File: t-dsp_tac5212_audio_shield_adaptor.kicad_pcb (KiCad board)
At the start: 2 copper layers, 26.5 x 60.9 mm, 22 parts, among them U1 Teensy 4.1 - DEVKIT

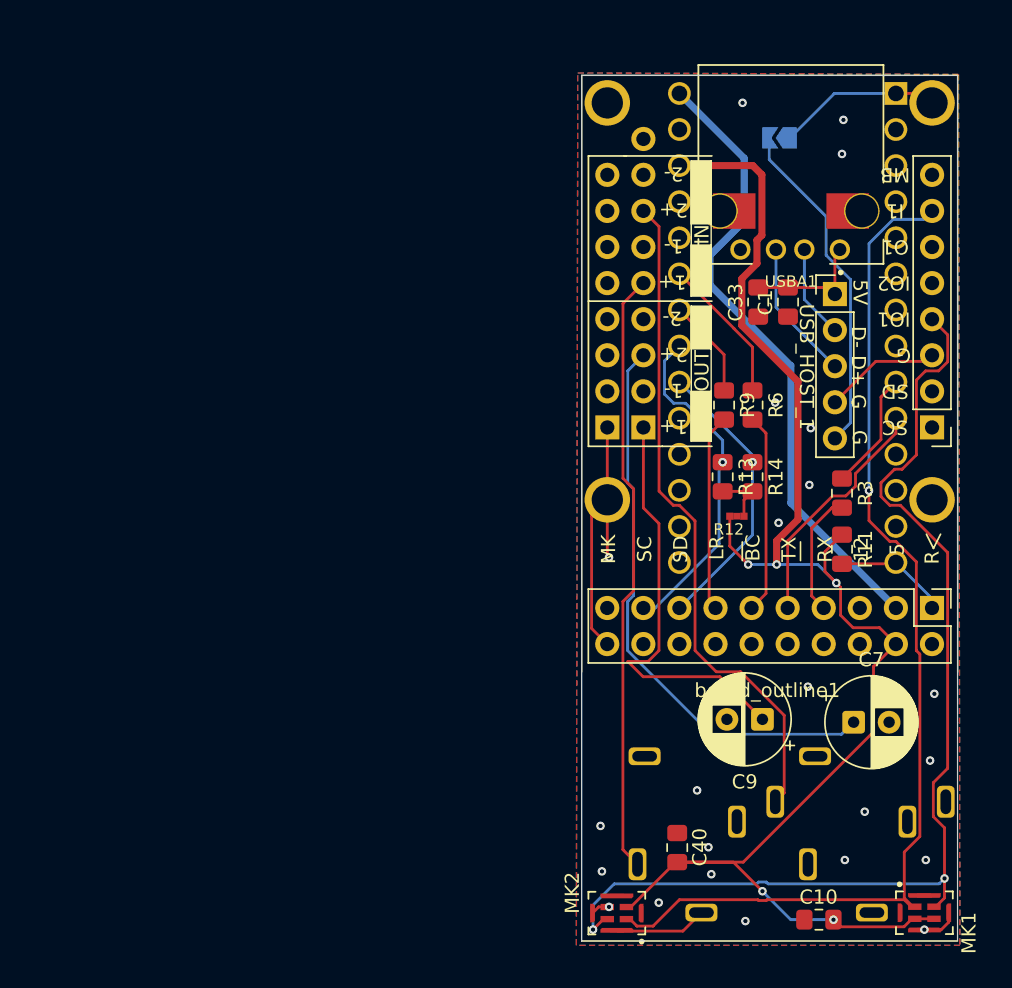
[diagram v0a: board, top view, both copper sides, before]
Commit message: v0.1: Finish routing, update board outline and revision
- Complete PCB routing and zone fills
- Add board outline footprint variants (-0.66mm offset)
- Update USB-A footprint to KiCad 9.0 format
- Fix schematic connections and capacitor orientation
- Correct project filename metadata
- Update 3D model
- Set REVISION to v0.1
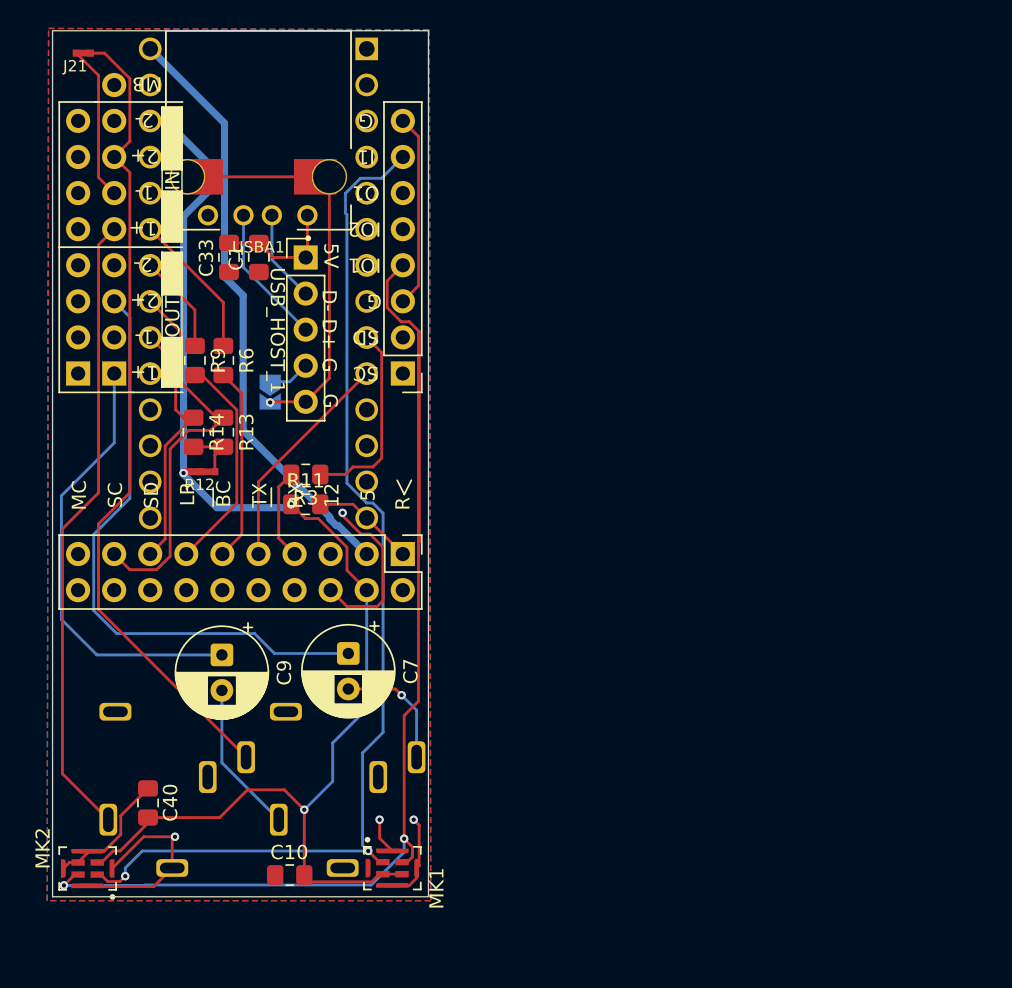
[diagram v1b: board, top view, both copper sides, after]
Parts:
- added J21: jumper, project_fp:jumper_slice, F.Cu at (99.7, 142.6)
- board_outline1: footprint project_fp:audio_module_board_outline_50x34.5_d1_ADAPTOR -> project_fp:audio_module_board_outline_final_minus-.66_mod_long
- moved G1 40.1 mm to (112.8, 166.5), turned to -90 degrees
- moved R14 39.5 mm to (107.5, 169.3)
- moved C9 38.3 mm to (109.5, 185.0), turned to -90 degrees
- moved R11 37.9 mm to (115.3, 174.4), turned to 0 degrees
- moved R3 37.8 mm to (115.3, 172.3), turned to 180 degrees
- moved MK1 37.6 mm to (121.5, 200.0)
- moved USBA1 37.6 mm to (112.0, 141.0)
- moved board_outline1 37.4 mm to (122.2, 180.4)
- moved C1 37.4 mm to (112.0, 157.0)
- moved HPTRS1 37.4 mm to (118.0, 202.0)
- moved HPTRS2 37.4 mm to (106.0, 202.0)
- moved R6 37.4 mm to (109.5, 164.2)
- moved R9 37.4 mm to (107.5, 164.2)
- moved U1 37.4 mm to (119.6, 142.3)
- moved C10 37.4 mm to (114.2, 200.5)
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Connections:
- HPTRS1 pad 2: Net-(HPTRS1-Pad2) -> Net-(C7-Pad2)
- HPTRS1 pad 5: Net-(HPTRS1-Pad5) -> Net-(C9-Pad2)
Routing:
- net 3.3V: track 107.9 -> 93.5 mm, vias 5 -> 3
- net GPIO1: track 76.8 -> 88.0 mm
- net Net-(board_outline1-IN1M): track 0.00 -> 11.0 mm
- net Net-(C9-Pad2): track 0.00 -> 10.8 mm
- net GND: track 50.6 -> 60.8 mm, vias 23 -> 4
- net /AUDIO_IN2P: track 47.2 -> 57.4 mm
- net Net-(C7-Pad2): track 0.00 -> 8.73 mm, vias 0 -> 1
- net Net-(U1-7_RX2_OUT1A): track 8.36 -> 13.7 mm
- net USB_SHIELD2: track 24.0 -> 29.3 mm, vias 0 -> 1
- net SCL0: track 23.9 -> 27.6 mm, vias 1 -> 0
- net 5V: track 44.5 -> 41.9 mm
- net 7_OUT1A: track 8.71 -> 6.43 mm
- net /AUDIO_OUT2P: track 40.3 -> 42.5 mm
- net SDA0: track 20.2 -> 18.2 mm, vias 1 -> 0
- net /AUDIO_IN1P: track 42.6 -> 44.4 mm
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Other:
- board size 26.5 x 60.9 mm -> 26.5 x 61 mm

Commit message: update
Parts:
- USB_HOST_1: moved to B.Cu
- turned USB_HOST_1 to 180 degrees
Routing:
- net USB_SHIELD2: track 29.3 -> 2.78 mm
- net 3.3V: track 93.5 -> 95.0 mm
